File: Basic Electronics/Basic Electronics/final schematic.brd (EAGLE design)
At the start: 38.1 x 43.2 mm, 9 parts, among them U1 SWITCH-SPST-2TV

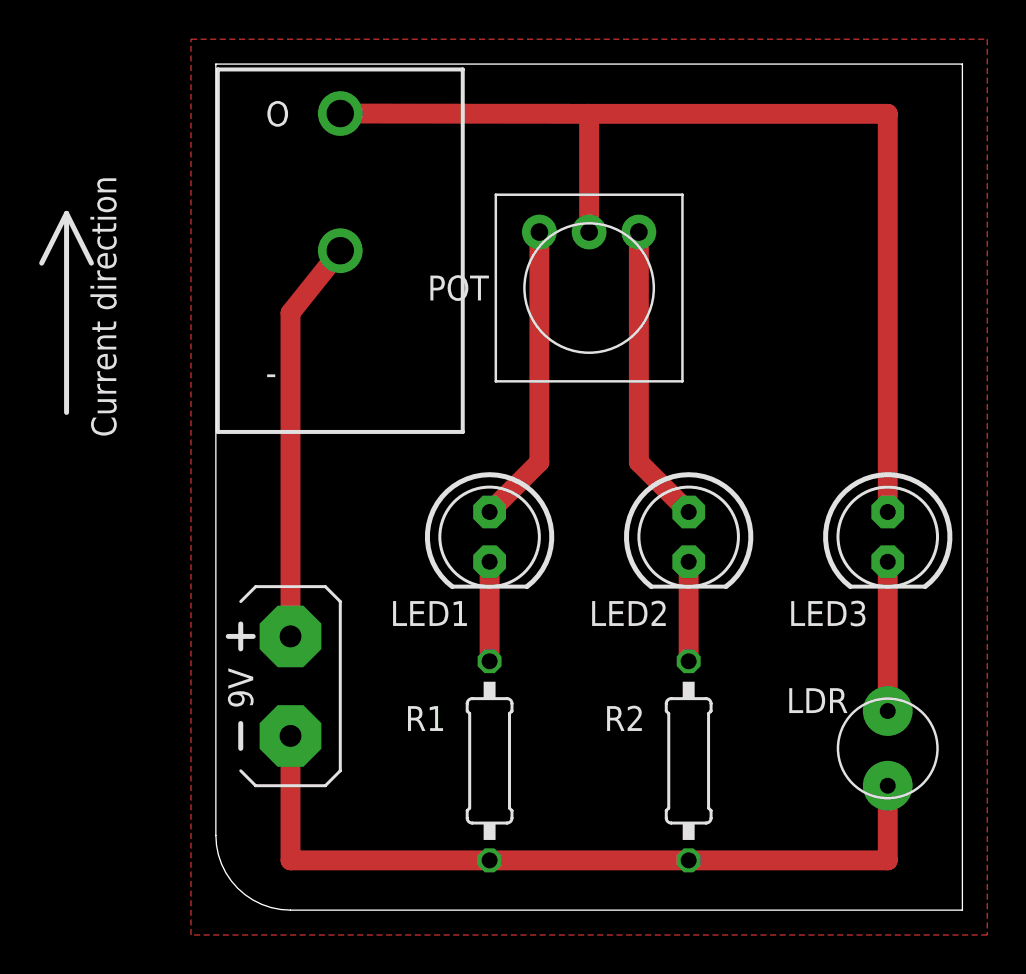
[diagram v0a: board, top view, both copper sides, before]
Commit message: added descriptions and thumbnails for website
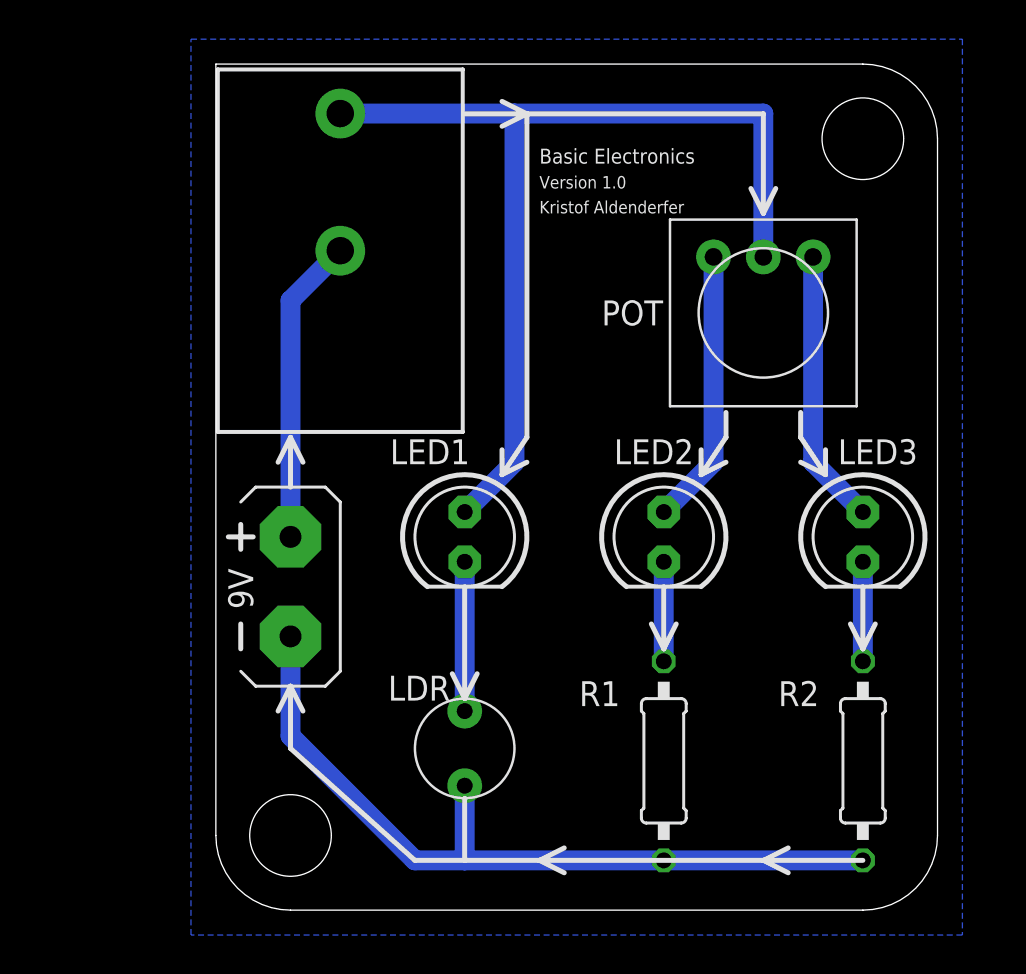
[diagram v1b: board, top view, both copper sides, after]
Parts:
- U1: device SparkFun-Electromechanical:SWITCH-SPST-VERTICAL -> personal:SWITCH-SPST-VERTICAL
- moved LDR 21.6 mm to (12.7, 8.26)
- moved POT 8.98 mm to (27.9, 30.5)
- moved R2 8.89 mm to (33.0, 7.62)
- moved R1 8.89 mm to (22.9, 7.62)
- moved G1 5.08 mm to (3.81, 16.5)
- moved LED1 1.27 mm to (12.7, 19.1)
- moved LED2 1.27 mm to (22.9, 19.1)
- moved LED3 1.27 mm to (33.0, 19.1)
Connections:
- net N$10: now also LED2.K; no longer LED1.K
- net N$2: now also LED1.A; no longer LED3.A
- net N$3: now also LED1.K; no longer LED3.K
- net N$5: now also LED3.K; no longer LED2.K
- net N$6: now also LED3.A; no longer LED2.A
- net N$7: now also LED2.A; no longer LED1.A
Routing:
- net N$9: track 20.6 -> 15.7 mm
- net N$2: track 54.3 -> 50.3 mm
- net N$7: track 15.3 -> 14.1 mm
- net N$6: track 15.3 -> 14.1 mm
- added copper zone on layer 16, net N$8
- removed copper zone on layer 1, net N$8
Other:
- board size 38.1 x 43.2 mm -> 36.8 x 43.2 mm
- board text added: "(Arrows indicate current direction)"
- board text added: "- battery +"
- board text added: "Basic Electronics"
- board text added: "Kristof Aldenderfer"
- board text added: "Version 1.0"
- board text removed: "Current direction"
- board text removed: "battery"
